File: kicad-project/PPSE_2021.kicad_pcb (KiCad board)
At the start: 2 copper layers, 100 x 60 mm, 129 parts, among them J1 Conn_02x04_Counter_Clockwise, J10 Motor 2, J2 Conn_02x08_Counter_Clockwise, J3 USB_B_Mini, J4 12V IN, J5 Compass, J6 Accelerometer, J7 OLED, J8 Screw_Terminal_01x04, J9 Motor 1, Q1 3LP01M, Q10 SI2300DS, Q11 SI2300DS, Q12 SI2300DS, Q13 SI2300DS, Q2 PDTC114Y, Q3 BC846A, Q4 BC846A, Q5 BC846A, Q6 SI2300DS, Q7 SI2300DS, Q8 SI2300DS, Q9 SI2300DS, SW1 PRG_SW, SW2 RST_SW, SW3 HOME_SW, SW4 EN_SW, U1 W25Q16JVSS, U2 RP2040, U3 TPS563201, U4 PAM-7Q-0, Y1 12MHz

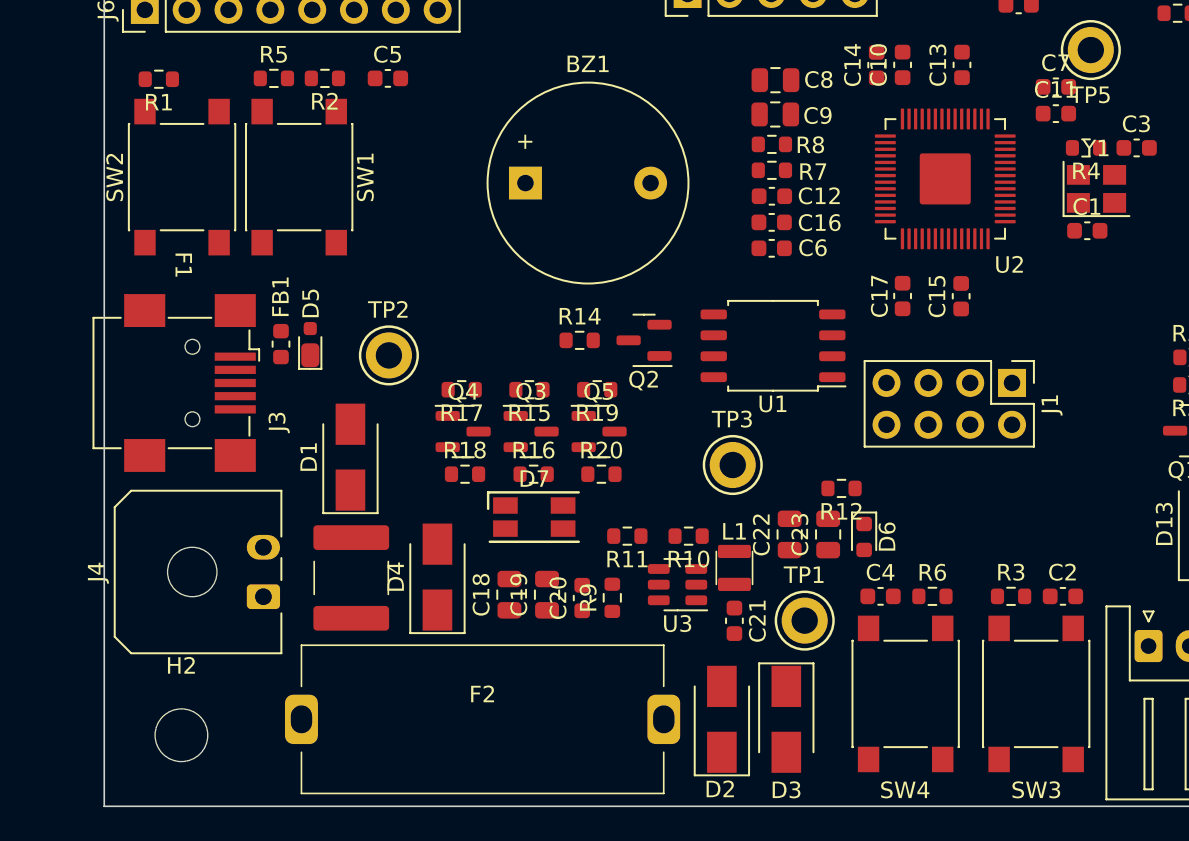
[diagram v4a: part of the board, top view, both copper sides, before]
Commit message: hw: add fiducial to eeschema and change sw footprints
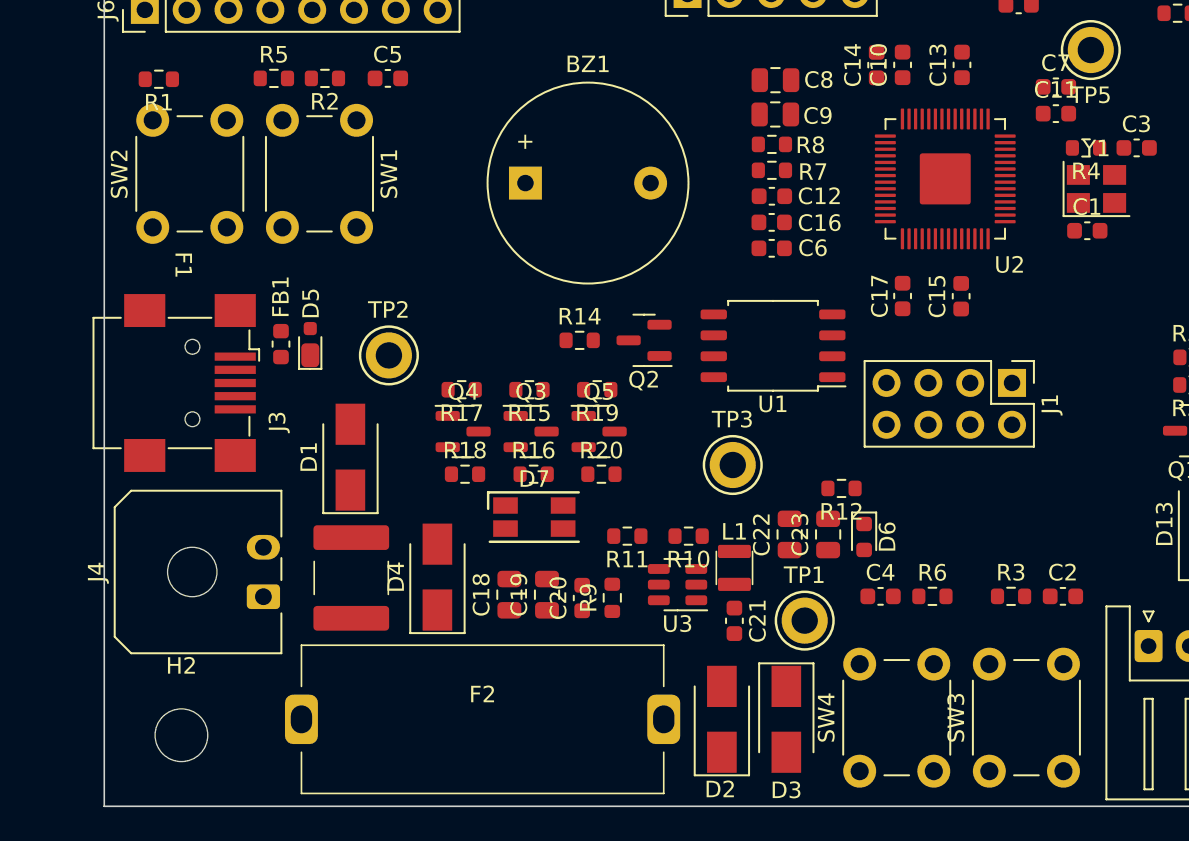
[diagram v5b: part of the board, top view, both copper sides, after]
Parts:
- SW1, SW2, SW3, SW4: footprint Button_Switch_SMD:SW_SPST_PTS645 -> Button_Switch_THT:SW_PUSH_6mm
- moved SW3 5.49 mm to (141.3, 132.8)
- moved SW4 5.46 mm to (133.4, 132.8)
- moved SW1 4.90 mm to (102.8, 93.3)
- moved SW2 3.53 mm to (90.5, 99.8)

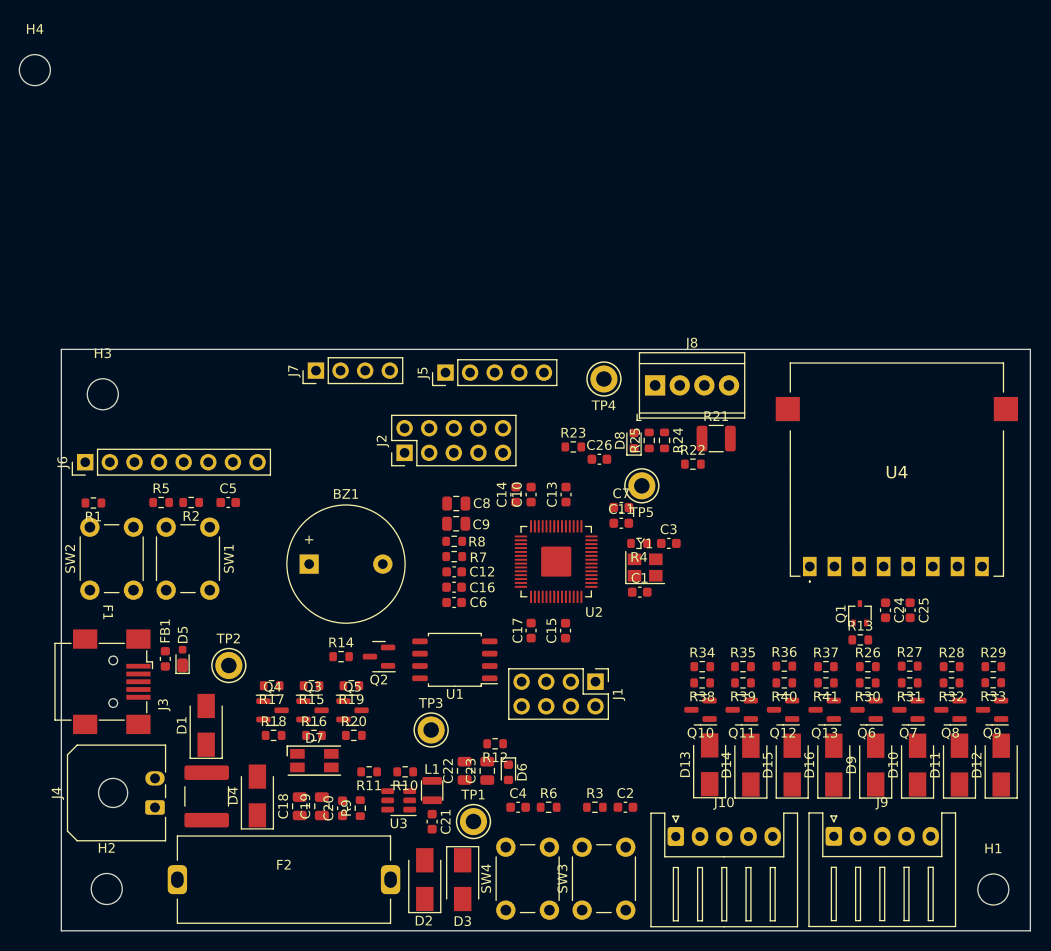
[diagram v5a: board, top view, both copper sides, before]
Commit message: change mcu pins and optimize layout
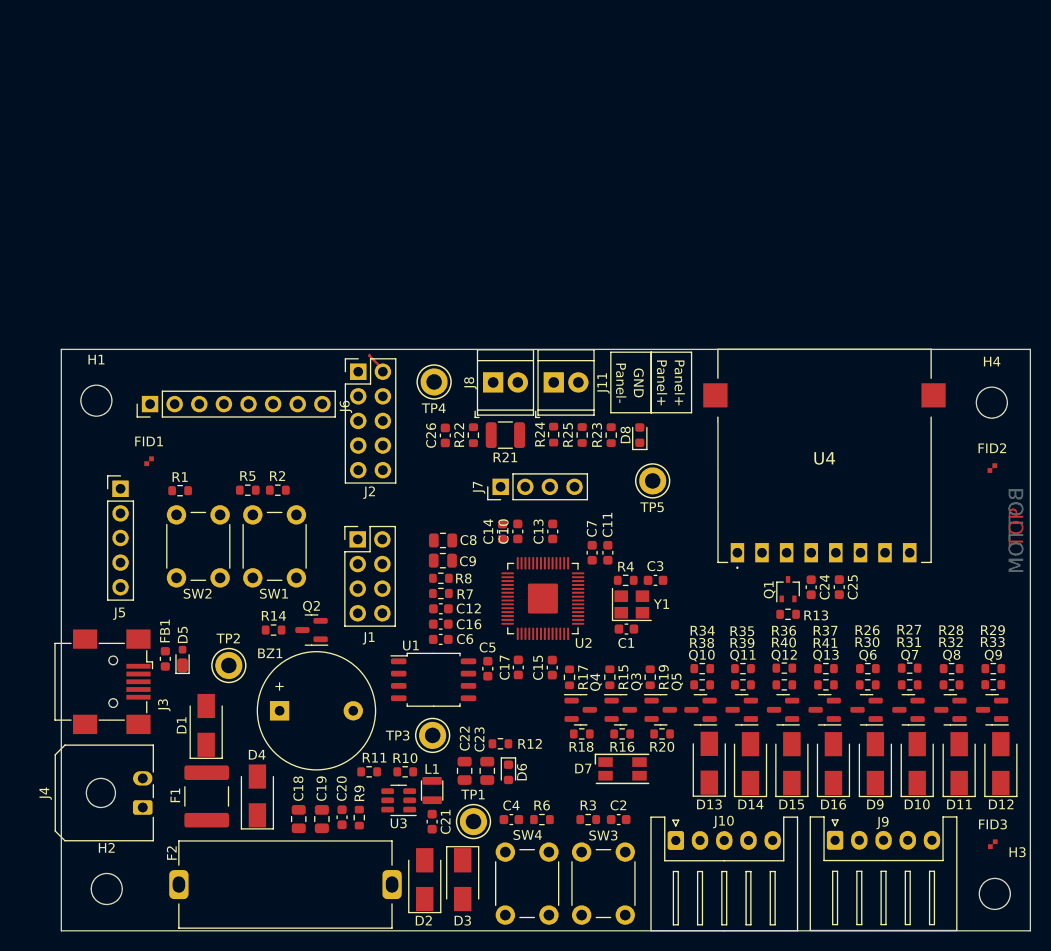
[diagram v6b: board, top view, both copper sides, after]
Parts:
- added FID1: Fiducial, ppse_2021:Fiducial-ppse, F.Cu at (96.6, 86.5)
- added FID2: Fiducial, ppse_2021:Fiducial-ppse, F.Cu at (183.6, 87.2)
- added FID3: Fiducial, ppse_2021:Fiducial-ppse, F.Cu at (183.6, 126.0)
- added J11: Panel+ Connector, TerminalBlock_TE-Connectivity:TerminalBlock_TE_282834-2_1x02_P2.54mm_Horizontal, F.Cu at (138.3, 78.3)
- J8: value Screw_Terminal_01x04 -> Panel- Connector; footprint TerminalBlock_TE-Connectivity:TerminalBlock_TE_282834-4_1x04_P2.54mm_Horizontal -> TerminalBlock_TE-Connectivity:TerminalBlock_TE_282834-2_1x02_P2.54mm_Horizontal
- moved H3 105.5 mm to (183.8, 131.1)
- moved H1 105.4 mm to (91.1, 80.2)
- moved H4 104.5 mm to (183.5, 80.4)
- moved J5 35.6 mm to (93.6, 89.3), turned to 0 degrees
- moved D7 31.8 mm to (145.4, 118.2)
- moved C5 31.8 mm to (131.5, 107.9), turned to -90 degrees
- moved R20 31.8 mm to (149.5, 114.6)
- moved R16 31.8 mm to (145.4, 114.6)
- moved R18 31.8 mm to (141.2, 114.6)
- moved Q3 31.8 mm to (145.2, 112.1)
- moved Q4 31.8 mm to (141.1, 112.1)
- moved Q5 31.8 mm to (149.4, 112.1)
- moved R19 30.8 mm to (148.3, 108.8), turned to -90 degrees
- moved R15 30.8 mm to (144.1, 108.8), turned to -90 degrees
- moved R17 30.7 mm to (140.0, 108.8), turned to -90 degrees
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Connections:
- J2 pad 10: /Connectivity/SDA -> /Control/EXT_ADC0
- J2 pad 2: /Control/GPIO6 -> /Control/GPIO4
- J2 pad 3: /Control/GPIO23 -> GND
- J2 pad 4: /Control/GPIO24 -> /Control/GPIO3
- J2 pad 5: /Control/GPIO25 -> /Connectivity/SCL
- J2 pad 6: GND -> /Control/GPIO2
- J2 pad 7: /Control/EXT_ADC1 -> /Connectivity/SDA
- J2 pad 8: /Control/EXT_ADC0 -> /Control/GPIO1
- J2 pad 9: /Connectivity/SCL -> /Control/EXT_ADC1
- J8 pad 1: /Sensing/Panel IN + -> /Sensing/Panel-
- J8 pad 2: /Sensing/Panel IN - -> GND
- R21 pad 1: /Sensing/Panel IN - -> /Sensing/Panel-
- R22 pad 1: /Sensing/Panel IN - -> /Sensing/Panel-
- R24 pad 1: /Sensing/Panel IN + -> /Sensing/Panel+
- TP4 pad 1: /Sensing/Panel IN - -> /Sensing/Panel-
- U2 pad 11: /Control/LED_G -> /Control/LED_R
- U2 pad 13: /Control/~{HOME_SW} -> /Actuation/M2_W11
- U2 pad 14: /Control/~{EN_SW} -> /Actuation/M2_W12
- U2 pad 15: /Actuation/M1_W11 -> /Actuation/M2_W21
- U2 pad 16: /Actuation/M1_W12 -> /Actuation/M1_W22
- U2 pad 17: /Actuation/M1_W21 -> /Actuation/M1_W11
- U2 pad 18: /Actuation/M1_W22 -> /Actuation/M1_W12
- U2 pad 2: /Connectivity/GPS_RX -> /Connectivity/Buzzer
- U2 pad 27: /Actuation/M2_W11 -> /Actuation/M1_W21
- U2 pad 28: /Connectivity/Buzzer -> /Actuation/M2_W22
- U2 pad 29: /Connectivity/DRDY -> /Connectivity/SDA
- U2 pad 3: /Connectivity/GPS_TX -> /Control/GPIO1
- U2 pad 30: /Connectivity/ACC_INT -> /Connectivity/SCL
- U2 pad 31: /Actuation/M2_W12 -> /Connectivity/DRDY
- U2 pad 32: /Actuation/M2_W21 -> /Connectivity/ACC_INT
- U2 pad 34: /Actuation/M2_W22 -> /Connectivity/GPS_EN
- U2 pad 35: /Control/GPIO23 -> /Connectivity/GPS_TP
- U2 pad 36: /Control/GPIO24 -> /Connectivity/GPS_RX
- U2 pad 37: /Control/GPIO25 -> /Connectivity/GPS_TX
- U2 pad 4: /Connectivity/GPS_EN -> /Control/GPIO2
- U2 pad 5: /Connectivity/GPS_TP -> /Control/GPIO3
- U2 pad 6: /Connectivity/SDA -> /Control/GPIO4
- U2 pad 7: /Connectivity/SCL -> /Control/~{EN_SW}
- U2 pad 8: /Control/GPIO6 -> /Control/~{HOME_SW}
- U2 pad 9: /Control/LED_R -> /Control/LED_G
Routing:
- net /Control/GPIO4: track 0.00 -> 2.04 mm
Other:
- board text added: "BOTTOM"
- board text added: "Capire se ingombro è da una parte e dall'altra"
- board text added: "Controllare orientamento?"
- board text added: "Difficile da saldare ->"
- board text added: "GND"
- board text added: "IMU goes here"
- board text added: "Panel+"
- board text added: "Panel-"
- board text added: "TOP"

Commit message: hw: power routing
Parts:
- J5: footprint Connector_PinHeader_2.54mm:PinHeader_1x05_P2.54mm_Vertical -> Connector_PinHeader_2.54mm:PinHeader_1x05_P2.54mm_Horizontal
- J6: footprint Connector_PinHeader_2.54mm:PinHeader_1x08_P2.54mm_Vertical -> Connector_PinHeader_2.54mm:PinHeader_1x08_P2.54mm_Horizontal
- moved J5 11.3 mm to (97.6, 99.9), turned to 180 degrees
- moved FID1 6.40 mm to (90.2, 85.6)
- moved J6 4.51 mm to (97.0, 85.1)
- moved J7 2.71 mm to (135.6, 89.1)
- moved R1 2.21 mm to (102.0, 89.5)
- moved R2 2.21 mm to (112.1, 89.4)
- moved R5 2.21 mm to (109.0, 89.4)
- moved SW1 2.21 mm to (114.0, 92.0)
- moved SW2 2.21 mm to (101.6, 98.5)
- moved J1 0.76 mm to (118.9, 94.5)
- moved J2 0.76 mm to (118.9, 77.2)
- moved C25 0.05 mm to (167.7, 99.5)
- turned C15 to -90 degrees
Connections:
- net Net-(D1-Pad1) renamed /Power/12V_Post_PPTC
- net Net-(D2-Pad1) renamed /Power/12V_Post_Fuse
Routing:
- net +3V3: track 0.00 -> 266.1 mm
- net +12V: track 0.00 -> 68.6 mm, vias 0 -> 9
- net /Power/SW_VIN: track 0.00 -> 35.2 mm
- net +1V1: track 0.00 -> 29.7 mm
- net /Actuation/M1_OUT4: track 0.00 -> 14.6 mm
- net /Actuation/M2_OUT4: track 0.00 -> 14.2 mm
- net /Control/V_PANEL: track 0.00 -> 13.4 mm
- net /Sensing/Panel-: track 0.00 -> 13.3 mm
- net /Actuation/M1_OUT3: track 0.00 -> 13.0 mm
- net /Actuation/M2_OUT3: track 0.00 -> 12.6 mm
- net /Actuation/M2_OUT1: track 0.00 -> 12.2 mm
- net /Actuation/M1_OUT2: track 0.00 -> 12.1 mm
- net /Actuation/M2_OUT2: track 0.00 -> 12.0 mm
- net /Actuation/M1_OUT1: track 0.00 -> 11.9 mm
- net /Connectivity/GPS_VCC: track 0.00 -> 10.9 mm
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- added copper zone on B.Cu, net +12V
- added copper zone on F.Cu, net +3V3
- added copper zone on F.Cu, net /Power/12V_IN
- added copper zone on F.Cu, net /Power/12V_Post_Fuse
- added copper zone on F.Cu, net /Sensing/Panel+
- added copper zone on B.Cu, net GND
- added copper zone on F.Cu, net GND
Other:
- board text added: "Cambiare se serve"
- board text removed: "Capire se ingombro è da una parte e dall'altra"
- board text removed: "IMU goes here"
- board text removed: "Se non c'è spazio, cambiare fusibile"

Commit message: hw: first round of routing
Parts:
- moved J5 3.04 mm to (94.6, 99.9)
- moved J6 2.92 mm to (97.0, 82.2)
- moved C15 1.20 mm to (137.5, 108.8)
- moved C17 1.00 mm to (134.7, 108.7)
- moved R10 0.52 mm to (123.0, 118.0)
- moved R11 0.52 mm to (119.3, 118.0)
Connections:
- U2 pad 16: /Actuation/M1_W22 -> /Actuation/M2_W22
- U2 pad 28: /Actuation/M2_W22 -> /Actuation/M1_W22
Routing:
- net /Connectivity/DRDY: track 0.00 -> 47.6 mm, vias 0 -> 2
- net /Actuation/M1_W22: track 0.00 -> 46.1 mm, vias 0 -> 2
- net /Actuation/M1_W21: track 0.00 -> 41.6 mm, vias 0 -> 2
- net /Connectivity/GPS_TP: track 0.00 -> 37.9 mm, vias 0 -> 1
- net /Control/USB_D+: track 0.00 -> 37.2 mm, vias 0 -> 2
- net /Control/USB_D-: track 0.00 -> 36.9 mm, vias 0 -> 2
- net /Connectivity/ACC_INT: track 0.00 -> 36.0 mm, vias 0 -> 3
- net /Actuation/M1_W12: track 0.00 -> 35.8 mm, vias 0 -> 2
- net /Connectivity/GPS_EN: track 0.00 -> 34.1 mm, vias 0 -> 2
- net /Actuation/M1_W11: track 0.00 -> 31.6 mm, vias 0 -> 2
- net /Control/~{HOME_SW}: track 0.00 -> 30.3 mm, vias 0 -> 3
- net /Control/~{EN_SW}: track 0.00 -> 29.8 mm, vias 0 -> 3
- net /Actuation/M2_W22: track 0.00 -> 27.2 mm
- net /Connectivity/GPS_TX: track 0.00 -> 26.5 mm, vias 0 -> 1
- net /Actuation/M2_W21: track 0.00 -> 22.9 mm
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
